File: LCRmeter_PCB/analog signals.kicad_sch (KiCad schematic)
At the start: 53 parts, among them J5 LCR_input, J6 LCR_input, U10 LT6202, U11 LT6202, U12 LMH6645, U13 LT6202, U14 LT6202, U15 LMH6645, U4 74LVC1G66, U5 74LVC1G66, U6 74LVC1G66, U7 74LVC1G66, U8 74LVC1G66, U9 74LVC1G66

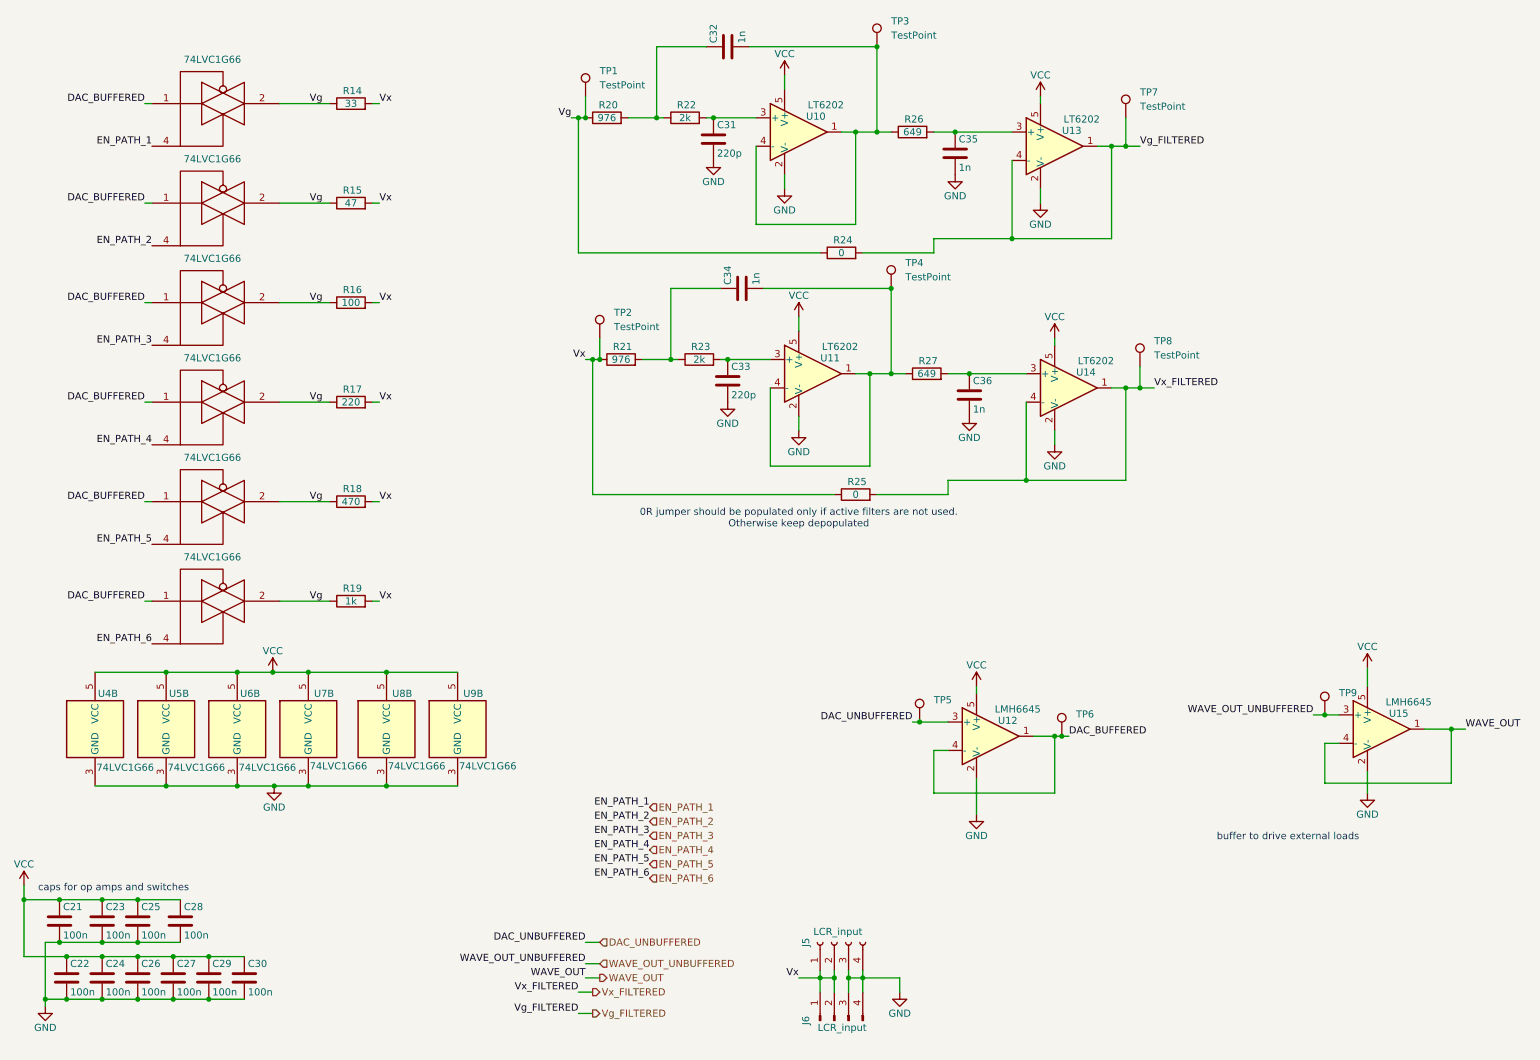
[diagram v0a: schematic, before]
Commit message: Fix TG connection for Vg; component placement; filter basis
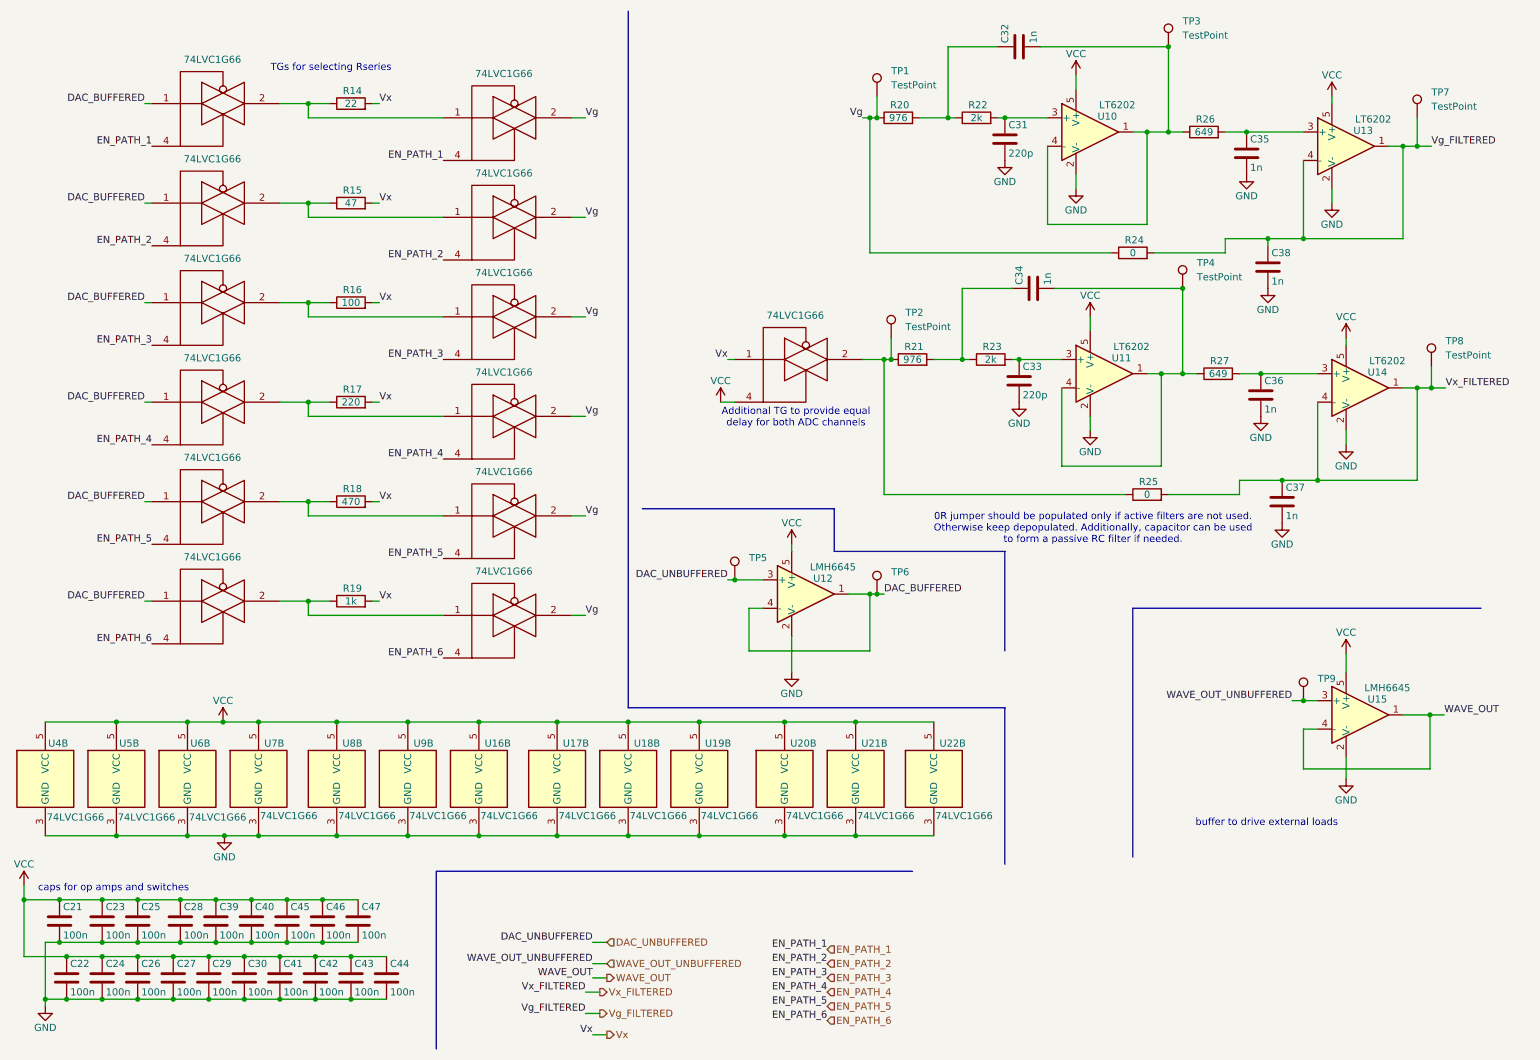
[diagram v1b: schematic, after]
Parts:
- removed J5: LCR_input, Connector_PinSocket_2.54mm:PinSocket_1x04_P2.54mm_Vertical, symbol lcrmeter-rescue:Conn_01x04_Female
- removed J6: LCR_input, Connector_PinHeader_2.54mm:PinHeader_1x04_P2.54mm_Vertical, symbol lcrmeter-rescue:Conn_01x04_Male
- added C37, C38: 1n, Capacitor_SMD:C_0402_1005Metric_Pad0.74x0.62mm_HandSolder, symbol Device:C
- added C39, C40, C41, C42, C43, C44, C45, C46, C47: 100n, Capacitor_SMD:C_0402_1005Metric_Pad0.74x0.62mm_HandSolder, symbol Device:C
- added U16, U17, U18, U19, U20, U21, U22: 74LVC1G66, Package_TO_SOT_SMD:SOT-23-5, symbol 74xGxx:74LVC1G66
- C21, C22, C23, C24, C25, C26, C27, C28, C29, C30, C31, C32, C33, C34, C35, C36: footprint Capacitor_SMD:C_0603_1608Metric_Pad1.08x0.95mm_HandSolder -> Capacitor_SMD:C_0402_1005Metric_Pad0.74x0.62mm_HandSolder
- R14: value 33 -> 22; footprint Resistor_SMD:R_0805_2012Metric_Pad1.20x1.40mm_HandSolder -> Resistor_SMD:R_0603_1608Metric_Pad0.98x0.95mm_HandSolder
- R15, R16, R17, R18, R19, R20, R21, R22, R23, R24, R25, R26, R27: footprint Resistor_SMD:R_0805_2012Metric_Pad1.20x1.40mm_HandSolder -> Resistor_SMD:R_0603_1608Metric_Pad0.98x0.95mm_HandSolder
- TP1, TP2, TP3, TP4, TP5, TP6, TP7, TP8, TP9: footprint (none) -> TestPoint:TestPoint_Pad_D1.5mm
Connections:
- net EN_PATH_1: now also U16.4
- net EN_PATH_2: now also U17.4
- net EN_PATH_3: now also U18.4
- net EN_PATH_4: now also U19.4
- net EN_PATH_5: now also U20.4
- net EN_PATH_6: now also U21.4
- net GND: now also C37.2, C38.2, C39.2, C40.2, C41.2, C42.2, C43.2, C44.2, C45.2, C46.2, C47.2, U16.3 (GND), U17.3 (GND), U18.3 (GND), U19.3 (GND), U20.3 (GND), U21.3 (GND), U22.3 (GND)
- net VCC: now also C39.1, C40.1, C41.1, C42.1, C43.1, C44.1, C45.1, C46.1, C47.1, U16.5 (VCC), U17.5 (VCC), U18.5 (VCC), U19.5 (VCC), U20.5 (VCC), U21.5 (VCC), U22.4, U22.5 (VCC)
- net Vg: now also U16.2, U17.2, U18.2, U19.2, U20.2, U21.2; no longer R14.1, R15.1, R16.1, R17.1, R18.1, R19.1, U4.2, U5.2, U6.2, U7.2, U8.2, U9.2
- net Vg_FILTERED: now also C38.1
- net Vx: now also U22.1; no longer R21.1, R25.1, TP2.1
- net Vx_FILTERED: now also C37.1
- new net: R16.1, U18.1, U5.2
- new net: R14.1, U16.1, U6.2
- new net: R21.1, R25.1, TP2.1, U22.2
- new net: R19.1, U21.1, U4.2
- new net: R17.1, U19.1, U8.2
- new net: R15.1, U17.1, U7.2
- new net: R18.1, U20.1, U9.2
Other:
- note added: "0R jumper should be populated only if active filters are not used. Otherwise keep depopulated. Additionally, capacitor can be used to form a passive RC filter if needed."
- note added: "Additional TG to provide equal delay for both ADC channels"
- note added: "TGs for selecting Rseries"
- note removed: "0R jumper should be populated only if active filters are not used. Otherwise keep depopulated"
- moved on the sheet: C31, C32, C33, C34, C35, C36, R20, R21, R22, R23, R24, R25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
